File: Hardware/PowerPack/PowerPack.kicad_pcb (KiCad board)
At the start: 4 copper layers, 45.6 x 25 mm, 51 parts, among them J2 529910208, J3 529910208, J4 XT30, U1 TPS2121RUXR, U2 LT6703CDC-3, U3 MAX77857, U5 MAX25232ATCB/V+T

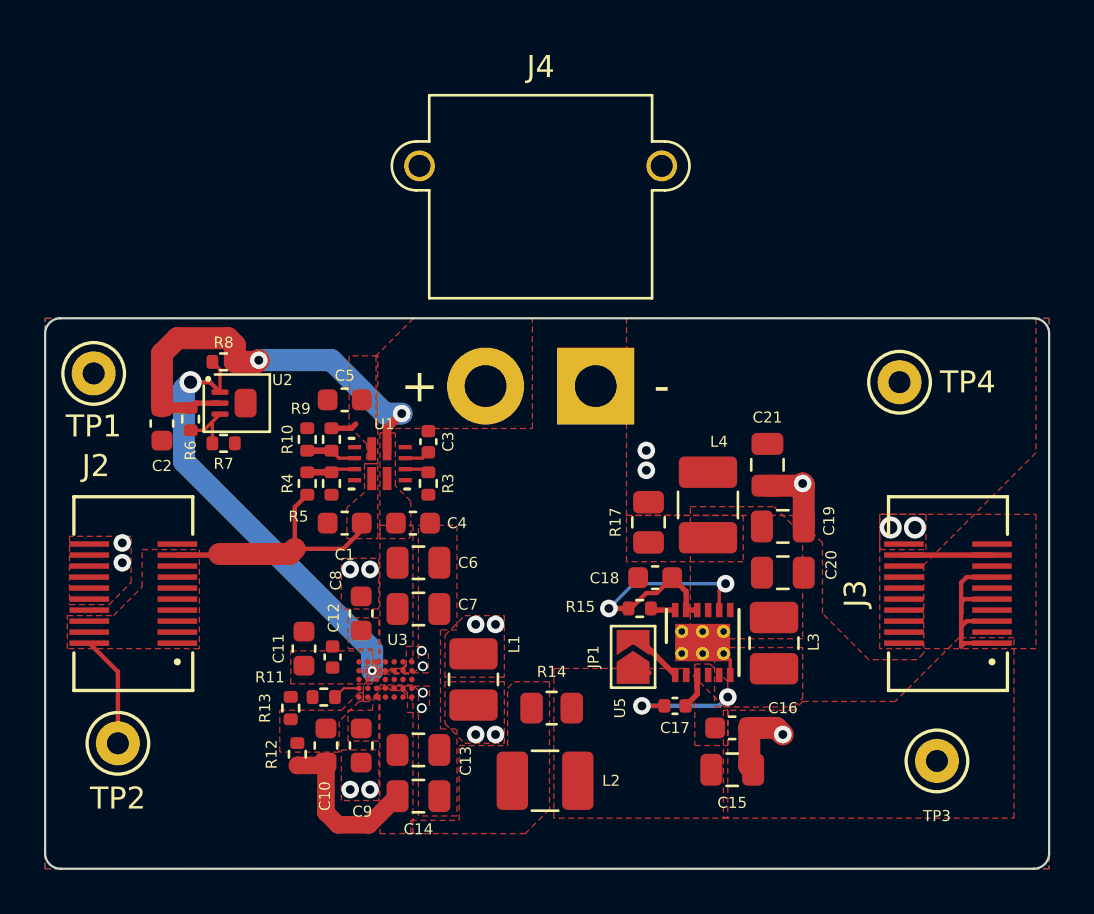
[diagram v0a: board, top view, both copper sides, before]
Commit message: flipped some connectors
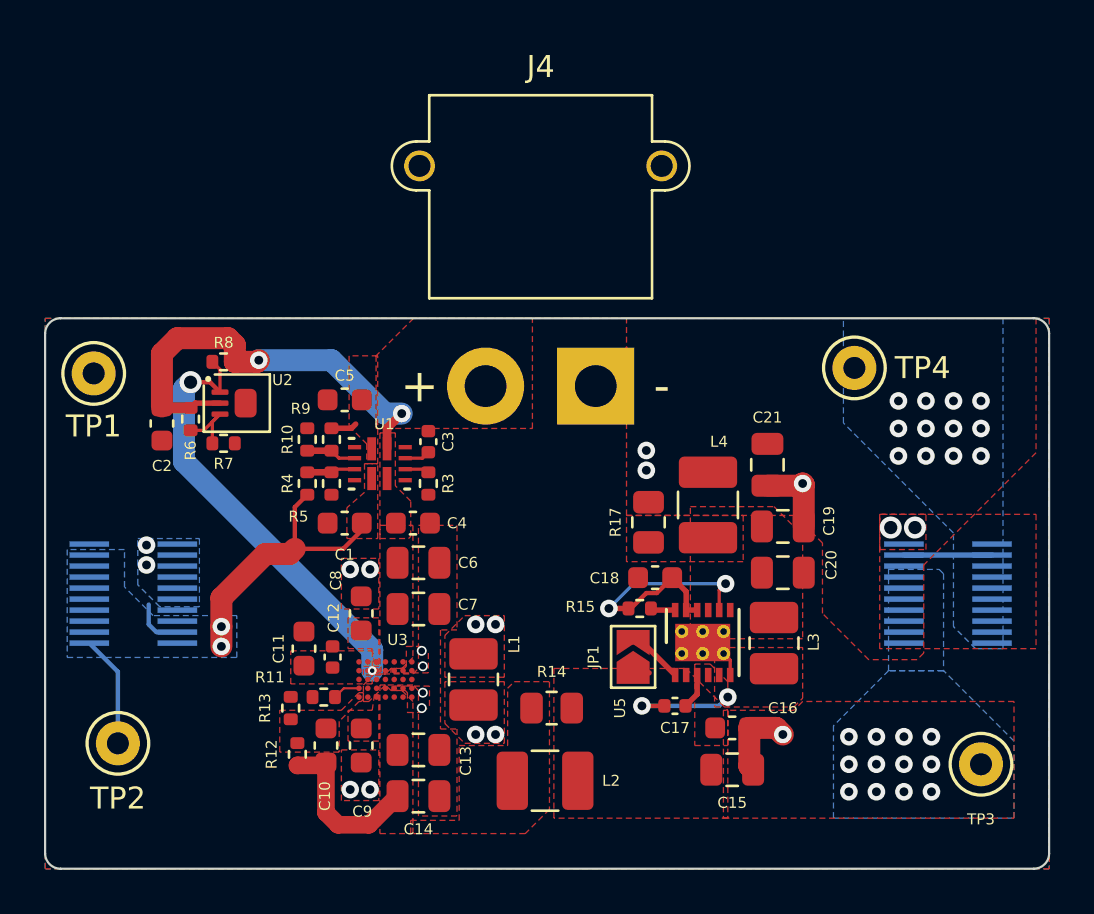
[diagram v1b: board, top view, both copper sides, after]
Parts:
- J2, J3: moved to B.Cu
- moved TP4 2.15 mm to (132.8, 52.8)
- moved TP3 2.01 mm to (138.5, 70.8)
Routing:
- net +5V: track 10.5 -> 0.72 mm, vias 0 -> 12
- net GND: track 8.33 -> 10.7 mm
- net VBUS: track 16.9 -> 18.0 mm, vias 0 -> 2
- net +3V3: vias 4 -> 16
- added copper zone on B.Cu, net +3V3
- added copper zone on B.Cu, net +5V
- added copper zone on B.Cu, net VBUS

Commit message: generating gerbers
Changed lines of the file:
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@@
       (plot_on_all_layers_selection 0x0000000_00000000)
       (disableapertmacros false)
-      (usegerberextensions false)
-      (usegerberattributes true)
-      (usegerberadvancedattributes true)
-      (creategerberjobfile true)
+      (usegerberextensions true)
+      (usegerberattributes false)
+      (usegerberadvancedattributes false)
+      (creategerberjobfile false)
       (dashed_line_dash_ratio 12.000000)
       (dashed_line_gap_ratio 3.000000)
@@
       (psa4output false)
       (plotreference true)
-      (plotvalue true)
+      (plotvalue false)
       (plotinvisibletext false)
       (sketchpadsonfab false)
-      (subtractmaskfromsilk false)
+      (subtractmaskfromsilk true)
       (outputformat 1)
       (mirror false)
-      (drillshape 1)
+      (drillshape 0)
       (scaleselection 1)
-      (outputdirectory "")
+      (outputdirectory "Gerber/")
     )
   )
@@
     (fp_line (start 1.25 1) (end -1.25 1)
       (stroke (width 0.1) (type solid)) (layer "F.Fab"))
-    (pad "1" smd roundrect (at -1.1625 0 90) (size 1.425 2.2) (layers "F.Cu" "F.Paste" "F.Mask") (roundrect_rratio 0.175439)
+    (pad "1" smd roundrect (at -1.1625 0 90) (size 1.425 2.2) (layers "F.Cu" "F.Paste" "F.Mask") (roundrect_rratio 0.1754392982)
       (net 15 "Net-(U5-LX)") (pintype "passive"))
-    (pad "2" smd roundrect (at 1.1625 0 90) (size 1.425 2.2) (layers "F.Cu" "F.Paste" "F.Mask") (roundrect_rratio 0.175439)
+    (pad "2" smd roundrect (at 1.1625 0 90) (size 1.425 2.2) (layers "F.Cu" "F.Paste" "F.Mask") (roundrect_rratio 0.1754392982)
       (net 17 "Net-(U5-OUT)") (pintype "passive"))
     (model "${KICAD6_3DMODEL_DIR}/Inductor_SMD.3dshapes/L_1008_2520Metric.wrl"
@@
     (fp_line (start 1.6 1.25) (end -1.6 1.25)
       (stroke (width 0.1) (type solid)) (layer "F.Fab"))
-    (pad "1" smd roundrect (at -1.4875 0 90) (size 1.425 2.65) (layers "F.Cu" "F.Paste" "F.Mask") (roundrect_rratio 0.175439)
+    (pad "1" smd roundrect (at -1.4875 0 90) (size 1.425 2.65) (layers "F.Cu" "F.Paste" "F.Mask") (roundrect_rratio 0.1754392982)
       (net 17 "Net-(U5-OUT)") (pinfunction "1") (pintype "passive"))
-    (pad "2" smd roundrect (at 1.4875 0 90) (size 1.425 2.65) (layers "F.Cu" "F.Paste" "F.Mask") (roundrect_rratio 0.175439)
+    (pad "2" smd roundrect (at 1.4875 0 90) (size 1.425 2.65) (layers "F.Cu" "F.Paste" "F.Mask") (roundrect_rratio 0.1754392982)
       (net 18 "+3V3") (pinfunction "2") (pintype "passive"))
     (model "${KICAD6_3DMODEL_DIR}/Inductor_SMD.3dshapes/L_1210_3225Metric.wrl"
@@
     (fp_line (start 1 0.625) (end -1 0.625)
       (stroke (width 0.1) (type solid)) (layer "F.Fab"))
-    (pad "1" smd roundrect (at -0.9125 0) (size 1.025 1.4) (layers "F.Cu" "F.Paste" "F.Mask") (roundrect_rratio 0.243902)
+    (pad "1" smd roundrect (at -0.9125 0) (size 1.025 1.4) (layers "F.Cu" "F.Paste" "F.Mask") (roundrect_rratio 0.243902439)
       (net 10 "Net-(C10-Pad1)") (pintype "passive"))
-    (pad "2" smd roundrect (at 0.9125 0) (size 1.025 1.4) (layers "F.Cu" "F.Paste" "F.Mask") (roundrect_rratio 0.243902)
+    (pad "2" smd roundrect (at 0.9125 0) (size 1.025 1.4) (layers "F.Cu" "F.Paste" "F.Mask") (roundrect_rratio 0.243902439)
       (net 13 "+5V") (pintype "passive"))
     (model "${KICAD6_3DMODEL_DIR}/Resistor_SMD.3dshapes/R_0805_2012Metric.wrl"
@@
     (fp_line (start 1.6 1.25) (end -1.6 1.25)
       (stroke (width 0.1) (type solid)) (layer "F.Fab"))
-    (pad "1" smd roundrect (at -1.4875 0) (size 1.425 2.65) (layers "F.Cu" "F.Paste" "F.Mask") (roundrect_rratio 0.175439)
+    (pad "1" smd roundrect (at -1.4875 0) (size 1.425 2.65) (layers "F.Cu" "F.Paste" "F.Mask") (roundrect_rratio 0.1754392982)
       (net 10 "Net-(C10-Pad1)") (pinfunction "1") (pintype "passive"))
-    (pad "2" smd roundrect (at 1.4875 0) (size 1.425 2.65) (layers "F.Cu" "F.Paste" "F.Mask") (roundrect_rratio 0.175439)
+    (pad "2" smd roundrect (at 1.4875 0) (size 1.425 2.65) (layers "F.Cu" "F.Paste" "F.Mask") (roundrect_rratio 0.1754392982)
       (net 13 "+5V") (pinfunction "2") (pintype "passive"))
     (model "${KICAD6_3DMODEL_DIR}/Inductor_SMD.3dshapes/L_1210_3225Metric.wrl"
@@
     (fp_line (start 1.25 1) (end -1.25 1)
       (stroke (width 0.1) (type solid)) (layer "F.Fab"))
-    (pad "1" smd roundrect (at -1.1625 0 270) (size 1.425 2.2) (layers "F.Cu" "F.Paste" "F.Mask") (roundrect_rratio 0.175439)
+    (pad "1" smd roundrect (at -1.1625 0 270) (size 1.425 2.2) (layers "F.Cu" "F.Paste" "F.Mask") (roundrect_rratio 0.1754392982)
       (net 7 "Net-(C8-Pad2)") (pinfunction "1") (pintype "passive"))
-    (pad "2" smd roundrect (at 1.1625 0 270) (size 1.425 2.2) (layers "F.Cu" "F.Paste" "F.Mask") (roundrect_rratio 0.175439)
+    (pad "2" smd roundrect (at 1.1625 0 270) (size 1.425 2.2) (layers "F.Cu" "F.Paste" "F.Mask") (roundrect_rratio 0.1754392982)
       (net 8 "Net-(C9-Pad1)") (pinfunction "2") (pintype "passive"))
     (model "${KICAD6_3DMODEL_DIR}/Inductor_SMD.3dshapes/L_1008_2520Metric.wrl"
@@
     (fp_line (start 1 0.625) (end -1 0.625)
       (stroke (width 0.1) (type solid)) (layer "F.Fab"))
-    (pad "1" smd roundrect (at -0.9125 0 90) (size 1.025 1.4) (layers "F.Cu" "F.Paste" "F.Mask") (roundrect_rratio 0.243902)
+    (pad "1" smd roundrect (at -0.9125 0 90) (size 1.025 1.4) (layers "F.Cu" "F.Paste" "F.Mask") (roundrect_rratio 0.243902439)
       (net 17 "Net-(U5-OUT)") (pintype "passive"))
-    (pad "2" smd roundrect (at 0.9125 0 90) (size 1.025 1.4) (layers "F.Cu" "F.Paste" "F.Mask") (roundrect_rratio 0.243902)
+    (pad "2" smd roundrect (at 0.9125 0 90) (size 1.025 1.4) (layers "F.Cu" "F.Paste" "F.Mask") (roundrect_rratio 0.243902439)
       (net 18 "+3V3") (pintype "passive"))
     (model "${KICAD6_3DMODEL_DIR}/Resistor_SMD.3dshapes/R_0805_2012Metric.wrl"

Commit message: generating some BOMs
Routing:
- net VBUS: track 18.0 -> 14.6 mm
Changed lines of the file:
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@@
   (segment (start 102.000001 64.750002) (end 101.050002 64.750002) (width 0.2) (layer "B.Cu") (net 2))
   (segment (start 107.333812 60.966188) (end 107.333812 59.076188) (width 0.2) (layer "F.Cu") (net 3))
-  (segment (start 110.375 60.125) (end 109.533812 60.966188) (width 0.2) (layer "F.Cu") (net 3))
   (segment (start 104 64.5) (end 104 65.4) (width 1) (layer "F.Cu") (net 3))
-  (segment (start 109.533812 60.966188) (end 107.333812 60.966188) (width 0.2) (layer "F.Cu") (net 3))
   (segment (start 110.375 59.8) (end 110.375 60.125) (width 0.15) (layer "F.Cu") (net 3))
   (segment (start 104 63.2) (end 104 64.5) (width 1) (layer "F.Cu") (net 3))
@@
       )
     )
+  )
+  (zone (net 3) (net_name "VBUS") (layer "F.Cu") (name "VBUS") (hatch edge 0.5)
+    (priority 27)
+    (connect_pads yes (clearance 0.13))
+    (min_thickness 0.25) (filled_areas_thickness no)
+    (fill yes (thermal_gap 0.5) (thermal_bridge_width 0.5))
+    (polygon
+      (pts
+        (xy 109.95 60.25)
+        (xy 109.45 60.75)
+        (xy 106 60.75)
+        (xy 106 62)
+        (xy 108.75 62)
+        (xy 109.5 61.25)
+        (xy 111 61.25)
+        (xy 111.1 61.15)
+        (xy 111.1 60.25)
+      )
+    )
